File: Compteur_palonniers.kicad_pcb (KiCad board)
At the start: 2 copper layers, 75 x 40 mm, 12 parts, among them J1 Conn_01x05, J101 Connecteur_Nextion, J2 Conn_01x04, K101 RelaisSRD, U1 MP1584, U2 µC

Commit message: Modif alim
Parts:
- D101: value 1N4148 -> Diode_1N4148
- U2: value µC -> ATtiny85
- moved J2 2.20 mm to (183.8, 101.2)
- moved D101 1.39 mm to (157.2, 101.2)
- moved K101 0.92 mm to (162.0, 99.0)
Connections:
- D101 pad 1: +24V -> 14
- J2 pad 4: Net-(J2-Pad4) -> 14
- K101 pad 14: Net-(J2-Pad4) -> 14
- K101 pad A2: +24V -> 14
- U1 pad 2: Net-(J2-Pad4) -> 14
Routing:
- net 14: track 0.00 -> 50.8 mm
- net Net-(J2-Pad4): track 49.5 -> 0.00 mm
- net +24V: track 190.8 -> 172.0 mm
- net Net-(D101-Pad2): track 32.0 -> 31.4 mm

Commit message: Version finale
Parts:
- moved D101 2.50 mm to (157.2, 98.7)
- moved E1 2.50 mm to (152.5, 107.5)
- moved J1 2.50 mm to (122.3, 98.6)
- moved J101 2.50 mm to (173.5, 121.7)
- moved J2 2.50 mm to (183.8, 98.7)
- moved K101 2.50 mm to (162.0, 96.5)
- moved R101 2.50 mm to (137.4, 116.1)
- moved R102 2.50 mm to (137.2, 111.9)
- moved R103 2.50 mm to (162.3, 110.1)
- moved TR101 2.50 mm to (183.2, 111.4)
- moved U1 2.50 mm to (140.1, 97.1)
- moved U2 2.50 mm to (152.3, 117.5)
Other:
- board size 75 x 40 mm -> 75 x 45 mm

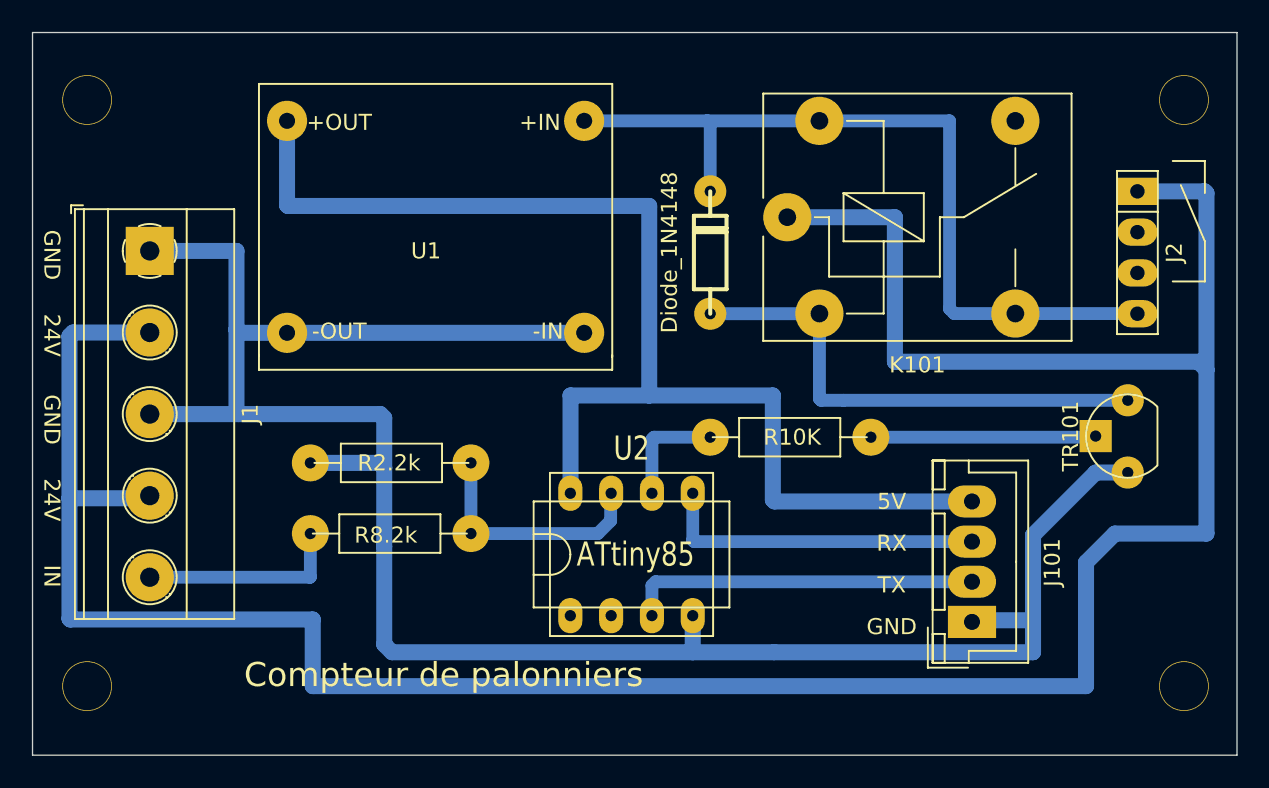
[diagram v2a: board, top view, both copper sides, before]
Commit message: Correction tracé pcb
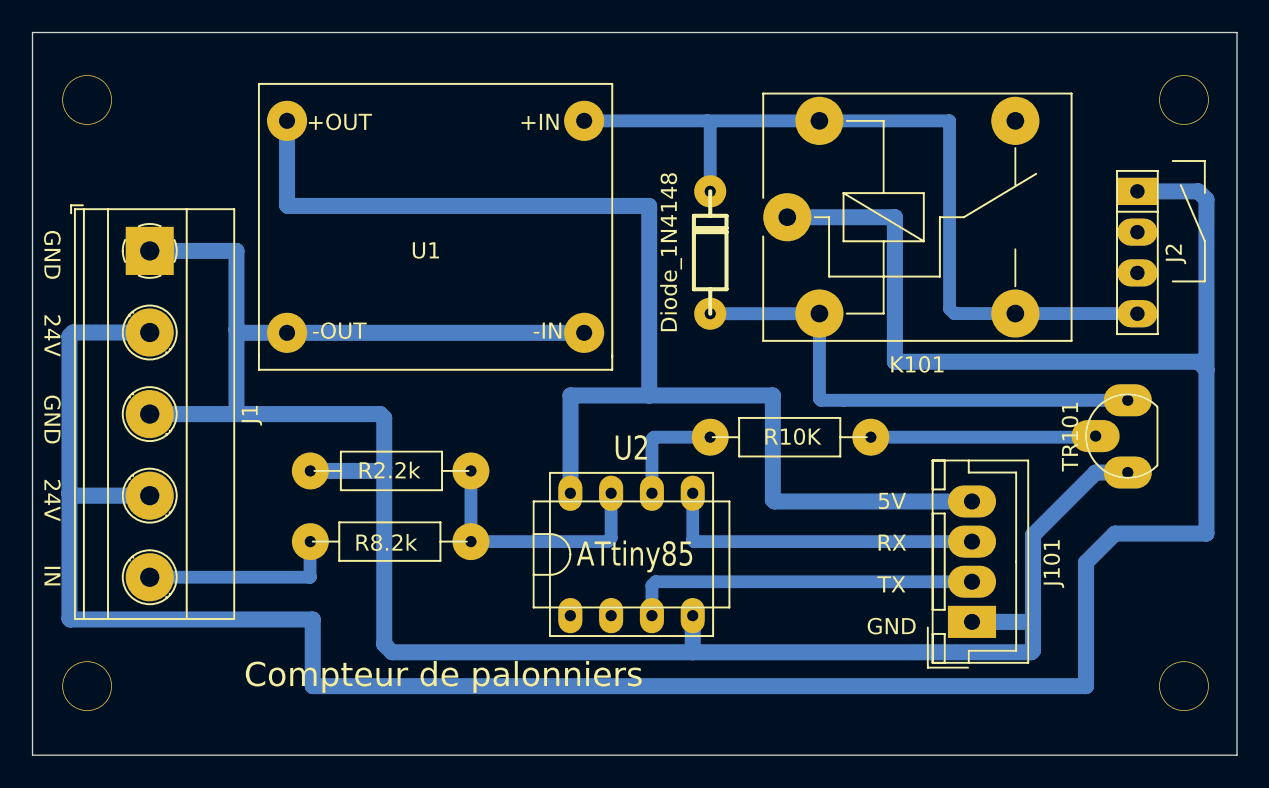
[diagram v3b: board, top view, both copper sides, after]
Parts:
- moved R101 0.50 mm to (137.4, 116.6)
- moved R102 0.50 mm to (137.2, 112.4)
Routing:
- net SIG: track 15.2 -> 16.0 mm
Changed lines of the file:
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@@
     (thickness 1.6)
     (drawings 19)
-    (tracks 98)
+    (tracks 95)
     (zones 0)
     (modules 12)
@@
     (mod_text_size 1 1)
     (mod_text_width 0.15)
-    (pad_size 1.524 1.524)
-    (pad_drill 0.762)
+    (pad_size 2 3)
+    (pad_drill 0.7)
     (pad_to_mask_clearance 0)
     (aux_axis_origin 115 130)
@@
       (effects (font (size 1 1) (thickness 0.15)))
     )
-    (pad 1 thru_hole circle (at -1 0 90) (size 2 2) (drill 0.7) (layers *.Cu *.Mask)
+    (pad 1 thru_hole oval (at -1 0 90) (size 2 3) (drill 0.7) (layers *.Cu *.Mask)
       (net 3 GND))
-    (pad 3 thru_hole circle (at 3.5 0 90) (size 2 2) (drill 0.7) (layers *.Cu *.Mask)
+    (pad 3 thru_hole oval (at 3.5 0 90) (size 2 3) (drill 0.7) (layers *.Cu *.Mask)
       (net 9 "Net-(D101-Pad2)"))
-    (pad 2 thru_hole rect (at 1.27 -2 90) (size 2 2) (drill 0.7) (layers *.Cu *.Mask)
+    (pad 2 thru_hole oval (at 1.27 -2 90) (size 2 3) (drill 0.7) (layers *.Cu *.Mask)
       (net 10 "Net-(R103-Pad2)"))
     (model ${KISYS3DMOD}/Transistor3d/TO-92.wrl
@@
   )
   (module Resistance:R_025W (layer F.Cu)
-    (at 137.2 111.9 180)
+    (at 137.2 112.4 180)
     (descr "Resistance 1/4w")
     (tags R)
@@
   )
   (module Resistance:R_025W (layer F.Cu)
-    (at 137.4 116.1)
+    (at 137.4 116.6)
     (descr "Resistance 1/4w")
     (tags R)
@@
   )
   (segment (start 122.3 118.92) (end 132.28 118.92) (width 0.8) (layer B.Cu) (net 1))
-  (segment (start 132.3 118.9) (end 132.3 116.2) (width 0.8) (layer B.Cu) (net 1))
   (segment (start 132.28 118.92) (end 132.3 118.9) (width 0.8) (layer B.Cu) (net 1))
+  (segment (start 132.28 116.72) (end 132.3 116.7) (width 0.8) (layer B.Cu) (net 1))
+  (segment (start 132.28 118.92) (end 132.28 116.72) (width 0.8) (layer B.Cu) (net 1))
   (segment (start 122.3 103.68) (end 117.52 103.68) (width 1) (layer B.Cu) (net 2))
-  (segment (start 117.52 103.68) (end 117.3 103.9) (width 1) (layer B.Cu) (net 2))
-  (segment (start 117.3 103.9) (end 117.3 114) (width 1) (layer B.Cu) (net 2))
-  (segment (start 122.14 114) (end 122.3 113.84) (width 1) (layer B.Cu) (net 2))
-  (segment (start 117.3 114) (end 122.14 114) (width 1) (layer B.Cu) (net 2))
   (segment (start 180.6 118) (end 182.4 116.2) (width 1) (layer B.Cu) (net 2))
   (segment (start 182.4 116.2) (end 188.1 116.2) (width 1) (layer B.Cu) (net 2))
@@
   (segment (start 117.349998 121.549998) (end 132.449998 121.549998) (width 1) (layer B.Cu) (net 2))
   (segment (start 117.3 121.5) (end 117.349998 121.549998) (width 1) (layer B.Cu) (net 2))
-  (segment (start 117.3 114) (end 117.3 121.5) (width 1) (layer B.Cu) (net 2))
-  (segment (start 187.99 94.89) (end 188.1 95) (width 1) (layer B.Cu) (net 2))
-  (segment (start 183.8 94.89) (end 187.99 94.89) (width 1) (layer B.Cu) (net 2))
   (segment (start 162 96.5) (end 168.7 96.5) (width 1) (layer B.Cu) (net 2))
   (segment (start 168.7 96.5) (end 168.7 105.5) (width 1) (layer B.Cu) (net 2))
   (segment (start 168.7 105.5) (end 187.6 105.5) (width 1) (layer B.Cu) (net 2))
-  (segment (start 188.1 106) (end 188.1 95) (width 1) (layer B.Cu) (net 2))
   (segment (start 187.6 105.5) (end 188.1 106) (width 1) (layer B.Cu) (net 2))
   (segment (start 188.1 116.2) (end 188.1 106) (width 1) (layer B.Cu) (net 2))
-  (segment (start 132.28 112.02) (end 132.3 112) (width 0.8) (layer B.Cu) (net 3))
-  (segment (start 137.39 123.59) (end 136.9 123.1) (width 1) (layer B.Cu) (net 3))
-  (segment (start 136.9 123.1) (end 136.9 117) (width 1) (layer B.Cu) (net 3))
-  (segment (start 156.11 123.59) (end 137.39 123.59) (width 1) (layer B.Cu) (net 3))
+  (segment (start 117.3 103.9) (end 117.52 103.68) (width 1) (layer B.Cu) (net 2))
+  (segment (start 117.44 113.84) (end 117.3 113.7) (width 1) (layer B.Cu) (net 2))
+  (segment (start 122.3 113.84) (end 117.44 113.84) (width 1) (layer B.Cu) (net 2))
+  (segment (start 117.3 113.7) (end 117.3 103.9) (width 1) (layer B.Cu) (net 2))
+  (segment (start 117.3 121.5) (end 117.3 113.7) (width 1) (layer B.Cu) (net 2))
+  (segment (start 188.1 106) (end 188.1 95.4) (width 1) (layer B.Cu) (net 2))
+  (segment (start 187.59 94.89) (end 183.8 94.89) (width 1) (layer B.Cu) (net 2))
+  (segment (start 188.1 95.4) (end 187.59 94.89) (width 1) (layer B.Cu) (net 2))
   (segment (start 156.11 121.31) (end 156.11 123.59) (width 1) (layer B.Cu) (net 3))
-  (segment (start 136.66 108.76) (end 136.9 109) (width 1) (layer B.Cu) (net 3))
   (segment (start 127.7 108.62) (end 127.84 108.76) (width 1) (layer B.Cu) (net 3))
-  (segment (start 127.84 108.76) (end 136.66 108.76) (width 1) (layer B.Cu) (net 3))
   (segment (start 122.3 108.76) (end 127.84 108.76) (width 1) (layer B.Cu) (net 3))
   (segment (start 122.3 98.6) (end 127.7 98.6) (width 1) (layer B.Cu) (net 3))
-  (segment (start 156.11 123.59) (end 161.19 123.59) (width 1) (layer B.Cu) (net 3))
-  (segment (start 182.9 112.7) (end 183.2 112.4) (width 1) (layer B.Cu) (net 3))
-  (segment (start 173.6 121.6) (end 173.5 121.7) (width 1) (layer B.Cu) (net 3))
-  (segment (start 177.3 121.6) (end 173.6 121.6) (width 1) (layer B.Cu) (net 3))
-  (segment (start 136.6 111.8) (end 136.9 112.1) (width 1) (layer B.Cu) (net 3))
-  (segment (start 132.3 111.8) (end 136.6 111.8) (width 1) (layer B.Cu) (net 3))
-  (segment (start 136.9 112.1) (end 136.9 117) (width 1) (layer B.Cu) (net 3))
-  (segment (start 136.9 109) (end 136.9 112.1) (width 1) (layer B.Cu) (net 3))
-  (segment (start 161.19 123.59) (end 177.29 123.59) (width 1) (layer B.Cu) (net 3))
-  (segment (start 177.3 123.58) (end 177.3 121.6) (width 1) (layer B.Cu) (net 3))
-  (segment (start 177.29 123.59) (end 177.3 123.58) (width 1) (layer B.Cu) (net 3))
   (segment (start 127.9 103.7) (end 127.7 103.5) (width 1) (layer B.Cu) (net 3))
   (segment (start 130.85 103.7) (end 127.9 103.7) (width 1) (layer B.Cu) (net 3))
@@
   (segment (start 149.35 103.7) (end 130.85 103.7) (width 1) (layer B.Cu) (net 3))
   (segment (start 177.3 116.3) (end 181.2 112.4) (width 1) (layer B.Cu) (net 3))
-  (segment (start 177.3 121.6) (end 177.3 116.3) (width 1) (layer B.Cu) (net 3))
   (segment (start 181.2 112.4) (end 183.2 112.4) (width 1) (layer B.Cu) (net 3))
+  (segment (start 136.66 108.76) (end 127.84 108.76) (width 1) (layer B.Cu) (net 3))
+  (segment (start 136.9 109) (end 136.66 108.76) (width 1) (layer B.Cu) (net 3))
+  (segment (start 137.39 123.59) (end 136.9 123.1) (width 1) (layer B.Cu) (net 3))
+  (segment (start 156.11 123.59) (end 137.39 123.59) (width 1) (layer B.Cu) (net 3))
+  (segment (start 132.3 112.3) (end 136.7 112.3) (width 1) (layer B.Cu) (net 3))
+  (segment (start 136.9 112.1) (end 136.9 109) (width 1) (layer B.Cu) (net 3))
+  (segment (start 136.7 112.3) (end 136.9 112.1) (width 1) (layer B.Cu) (net 3))
+  (segment (start 136.9 123.1) (end 136.9 112.1) (width 1) (layer B.Cu) (net 3))
+  (segment (start 177.2 121.7) (end 177.3 121.6) (width 1) (layer B.Cu) (net 3))
+  (segment (start 173.5 121.7) (end 177.2 121.7) (width 1) (layer B.Cu) (net 3))
+  (segment (start 177.3 123.48) (end 177.3 120.9) (width 1) (layer B.Cu) (net 3))
+  (segment (start 177.19 123.59) (end 177.3 123.48) (width 1) (layer B.Cu) (net 3))
+  (segment (start 156.11 123.59) (end 177.19 123.59) (width 1) (layer B.Cu) (net 3))
+  (segment (start 177.3 120.9) (end 177.3 116.3) (width 1) (layer B.Cu) (net 3))
+  (segment (start 177.3 121.6) (end 177.3 120.9) (width 1) (layer B.Cu) (net 3))
   (segment (start 161.1 114.1) (end 161.1 107.6) (width 1) (layer B.Cu) (net 4))
   (segment (start 161.2 114.2) (end 161.1 114.1) (width 1) (layer B.Cu) (net 4))
@@
   (segment (start 153.4 107.6) (end 148.5 107.6) (width 1) (layer B.Cu) (net 4))
   (segment (start 161.1 107.6) (end 153.4 107.6) (width 1) (layer B.Cu) (net 4))
-  (segment (start 173.35999 119.55999) (end 173.5 119.7) (width 0.8) (layer B.Cu) (net 5))
   (segment (start 173.5 119.2) (end 153.8 119.2) (width 0.8) (layer B.Cu) (net 5))
   (segment (start 153.57 119.43) (end 153.8 119.2) (width 0.8) (layer B.Cu) (net 5))
@@
   (segment (start 153.7 110.2) (end 153.57 110.33) (width 0.8) (layer B.Cu) (net 7))
   (segment (start 157.2 110.2) (end 153.7 110.2) (width 0.8) (layer B.Cu) (net 7))
-  (segment (start 142.3 111.8) (end 142.3 116.2) (width 0.8) (layer B.Cu) (net 8))
   (segment (start 151 113.72) (end 151.03 113.69) (width 0.8) (layer B.Cu) (net 8))
-  (segment (start 151 115.4) (end 151 113.72) (width 0.8) (layer B.Cu) (net 8))
-  (segment (start 150.2 116.2) (end 151 115.4) (width 0.8) (layer B.Cu) (net 8))
-  (segment (start 142.3 116.2) (end 150.2 116.2) (width 0.8) (layer B.Cu) (net 8))
+  (segment (start 142.3 116.7) (end 150.8 116.7) (width 0.8) (layer B.Cu) (net 8))
+  (segment (start 151.03 116.47) (end 151.03 113.69) (width 0.8) (layer B.Cu) (net 8))
+  (segment (start 150.8 116.7) (end 151.03 116.47) (width 0.8) (layer B.Cu) (net 8))
+  (segment (start 142.3 116.7) (end 142.3 112.3) (width 0.8) (layer B.Cu) (net 8))
   (segment (start 165.5 107.9) (end 183.2 107.9) (width 0.8) (layer B.Cu) (net 9))
   (segment (start 164.19 103.41) (end 164.2 103.4) (width 0.8) (layer B.Cu) (net 9))

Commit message: Version finale
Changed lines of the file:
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@@
     (descr "IC, DIL8 x 0,3\", with socket")
     (tags DIL)
-    (fp_text reference U2 (at 0 -6.6) (layer F.SilkS)
+    (fp_text reference U2 (at 0 -6.6) (layer F.SilkS) hide
       (effects (font (size 1.5 1.2) (thickness 0.15)))
     )
@@
     (effects (font (size 1.5 1.5) (thickness 0.3)))
   )
-  (gr_line (start 188 98) (end 186.5 94.5) (layer F.SilkS) (width 0.12))
-  (gr_line (start 188 100.5) (end 188 98) (layer F.SilkS) (width 0.12))
-  (gr_line (start 186 100.5) (end 188 100.5) (layer F.SilkS) (width 0.12))
-  (gr_line (start 188 93) (end 188 95) (layer F.SilkS) (width 0.12))
-  (gr_line (start 186 93) (end 188 93) (layer F.SilkS) (width 0.12))
+  (gr_line (start 188.6 100.1) (end 187.1 96.6) (layer F.SilkS) (width 0.12))
+  (gr_line (start 188.6 102.6) (end 188.6 100.1) (layer F.SilkS) (width 0.12))
+  (gr_line (start 186.6 102.6) (end 188.6 102.6) (layer F.SilkS) (width 0.12))
+  (gr_line (start 188.6 95.1) (end 188.6 97.1) (layer F.SilkS) (width 0.12))
+  (gr_line (start 186.6 95.1) (end 188.6 95.1) (layer F.SilkS) (width 0.12))
   (gr_text IN (at 116.2 118.85 -90) (layer F.SilkS)
     (effects (font (size 1 1) (thickness 0.15)))
